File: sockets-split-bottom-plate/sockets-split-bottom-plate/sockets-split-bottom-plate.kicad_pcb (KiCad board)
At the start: 2 copper layers, 138.1 x 85.2 mm, 0 parts

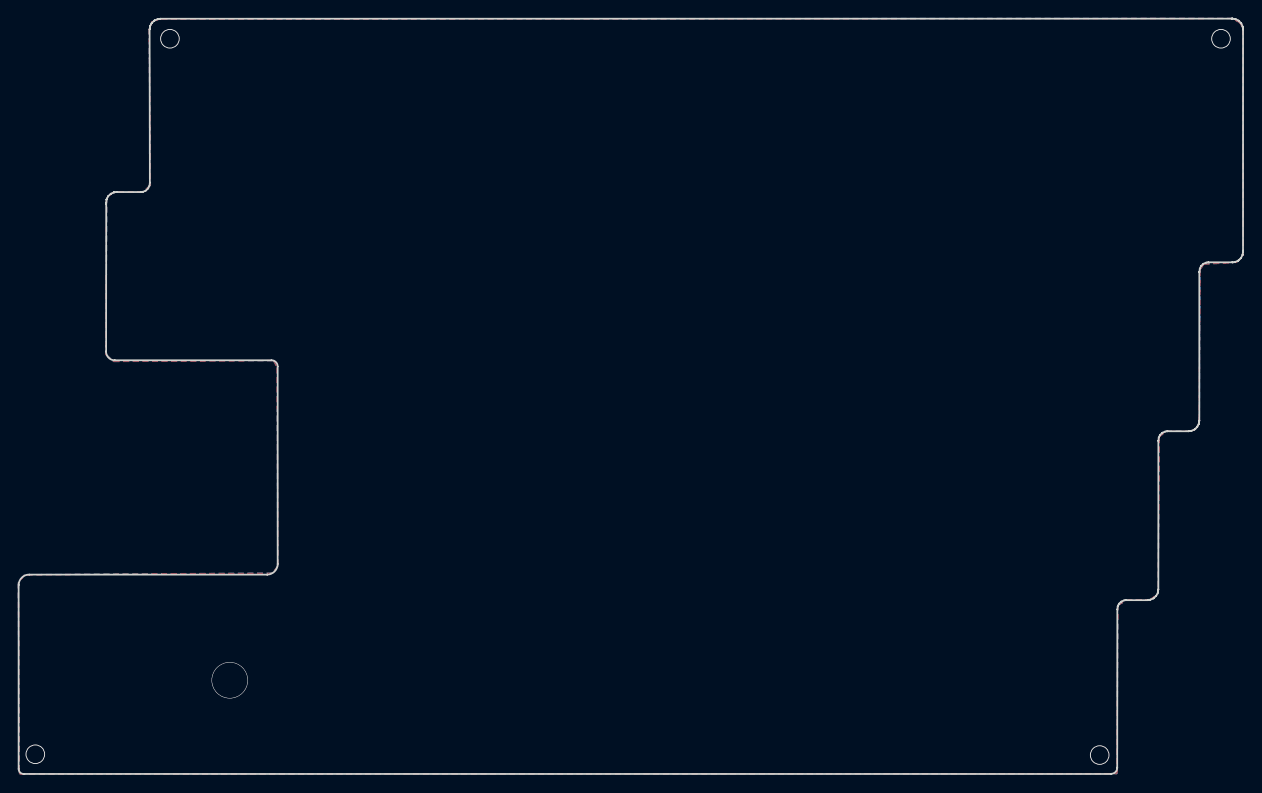
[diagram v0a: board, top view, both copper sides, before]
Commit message: 一発で生産できなかったので、pcbの修正
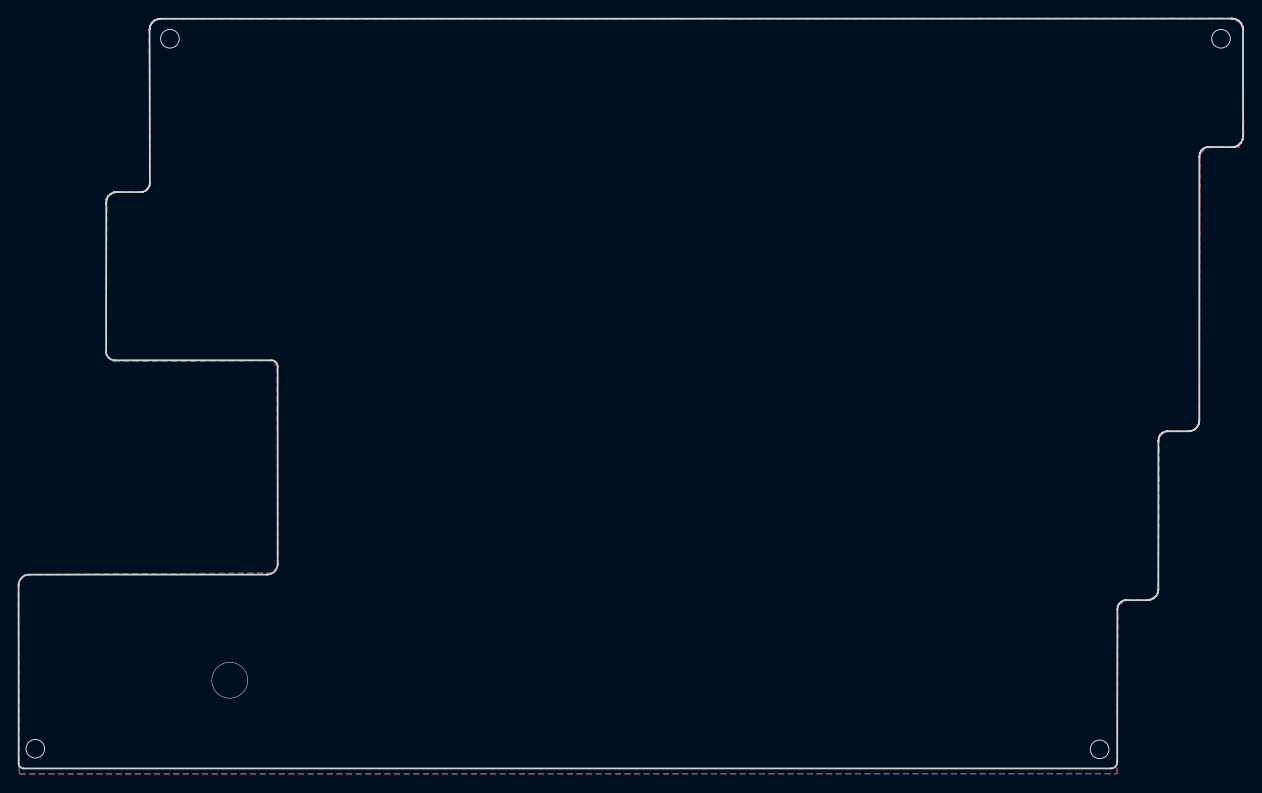
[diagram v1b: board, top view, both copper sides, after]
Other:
- board size 138.1 x 85.2 mm -> 138.1 x 84.6 mm
